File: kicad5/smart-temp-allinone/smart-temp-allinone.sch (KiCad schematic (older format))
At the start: 7 parts, among them J1 USB_A, J2 Conn_02x04_Odd_Even, J3 USB_A, J4 Conn_01x06_Female

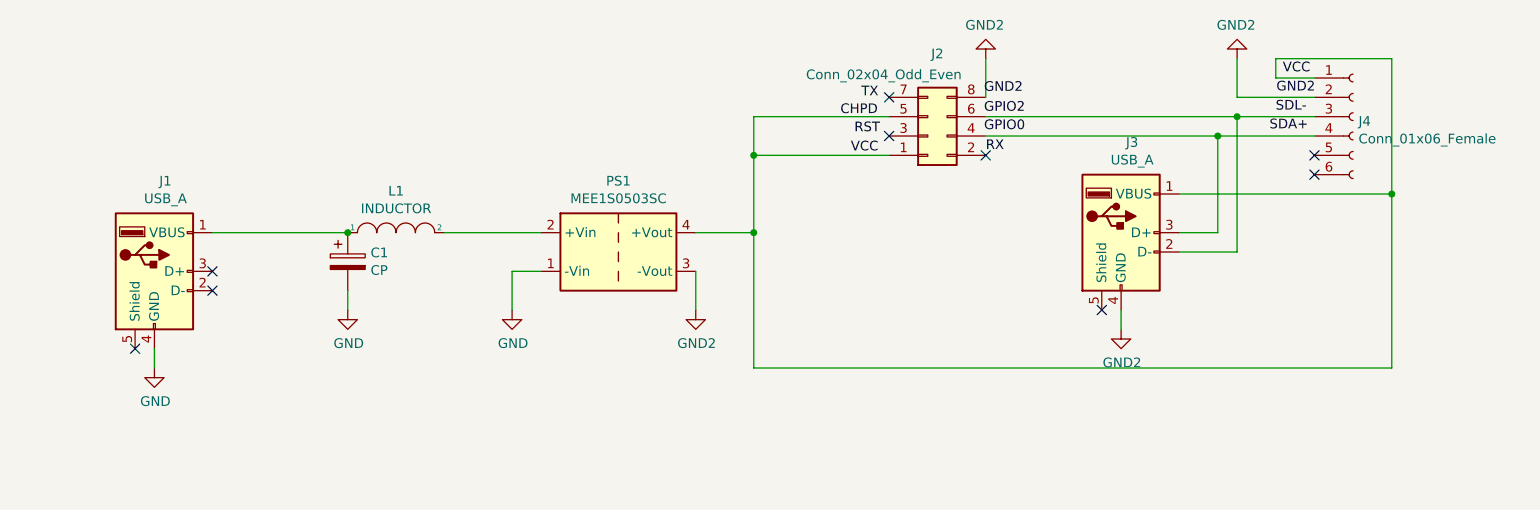
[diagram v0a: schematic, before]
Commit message: noid: changed female usb connect ids
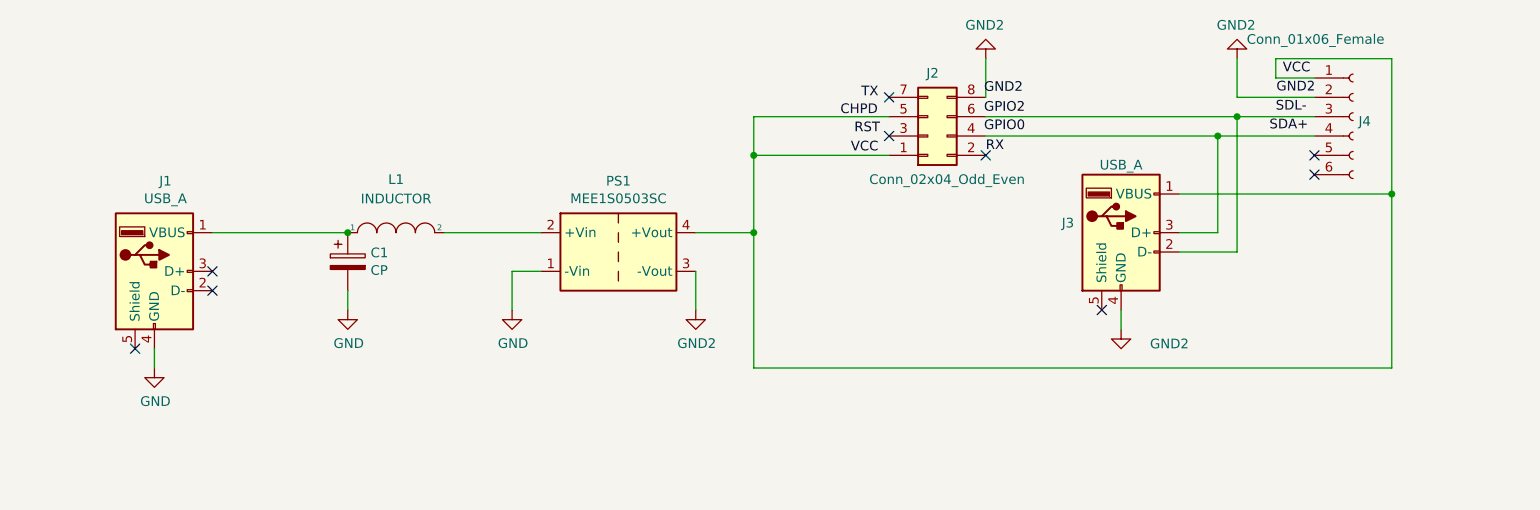
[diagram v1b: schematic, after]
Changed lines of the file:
@@
 U 1 1 63473160
 P 6700 3100
-F 0 "J2" H 6750 2675 50  0000 C CNN
-F 1 "Conn_02x04_Odd_Even" H 6473 2783 50  0000 C CNN
+F 0 "J2" H 6725 2775 50  0000 C CNN
+F 1 "Conn_02x04_Odd_Even" H 6800 3325 50  0000 C CNN
 F 2 "Connector_PinSocket_2.54mm:PinSocket_2x04_P2.54mm_Vertical" H 6700 3100 50  0001 C CNN
 F 3 "~" H 6700 3100 50  0001 C CNN
@@
 U 1 1 6348612A
 P 7700 3600
-F 0 "J3" H 7757 4067 50  0000 C CNN
-F 1 "USB_A" H 7757 3976 50  0000 C CNN
+F 0 "J3" H 7425 3650 50  0000 C CNN
+F 1 "USB_A" H 7700 3950 50  0000 C CNN
 F 2 "kicad3_footprint:USB_A_Molex_67643_Horizontal_femal" H 7850 3550 50  0001 C CNN
 F 3 " ~" H 7850 3550 50  0001 C CNN
@@
 P 8900 3000
 F 0 "J4" H 8928 2976 50  0000 L CNN
-F 1 "Conn_01x06_Female" H 8928 2885 50  0000 L CNN
+F 1 "Conn_01x06_Female" H 8350 3400 50  0000 L CNN
 F 2 "Connector_PinSocket_2.54mm:PinSocket_1x06_P2.54mm_Horizontal" H 8900 3000 50  0001 C CNN
 F 3 "~" H 8900 3000 50  0001 C CNN
@@
 P 7700 4100
 F 0 "#PWR0105" H 7700 3850 50  0001 C CNN
-F 1 "GND2" H 7705 3927 50  0000 C CNN
+F 1 "GND2" H 7950 4025 50  0000 C CNN
 F 2 "" H 7700 4100 50  0001 C CNN
 F 3 "" H 7700 4100 50  0001 C CNN
@@
 U 1 1 634BA9E4
 P 3950 3600
-F 0 "L1" H 3950 3815 50  0000 C CNN
-F 1 "INDUCTOR" H 3950 3724 50  0000 C CNN
+F 0 "L1" H 3950 3875 50  0000 C CNN
+F 1 "INDUCTOR" H 3950 3775 50  0000 C CNN
 F 2 "Inductor_THT:L_Radial_D12.5mm_P7.00mm_Fastron_09HCP" H 3950 3600 50  0001 C CNN
 F 3 "~" H 3950 3600 50  0001 C CNN

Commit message: noid: add pwr
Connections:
- net +5V: now reaches C1.1, J1.1 (VBUS), L1.1
- net +3V3: now reaches J2.1 (Pin_1), J2.5 (Pin_5), J3.1 (VBUS), J4.1 (Pin_1), PS1.4 (+Vout)
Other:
- moved on the sheet: C1, J2, J3, J4, L1, PS1
